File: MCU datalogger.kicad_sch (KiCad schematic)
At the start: 25 parts, among them U1 24LC1025, U2 24LC1025, U3 ATMEGA328P-AU, U4 DS1337S_, Y1 Crystal, Y2 Crystal

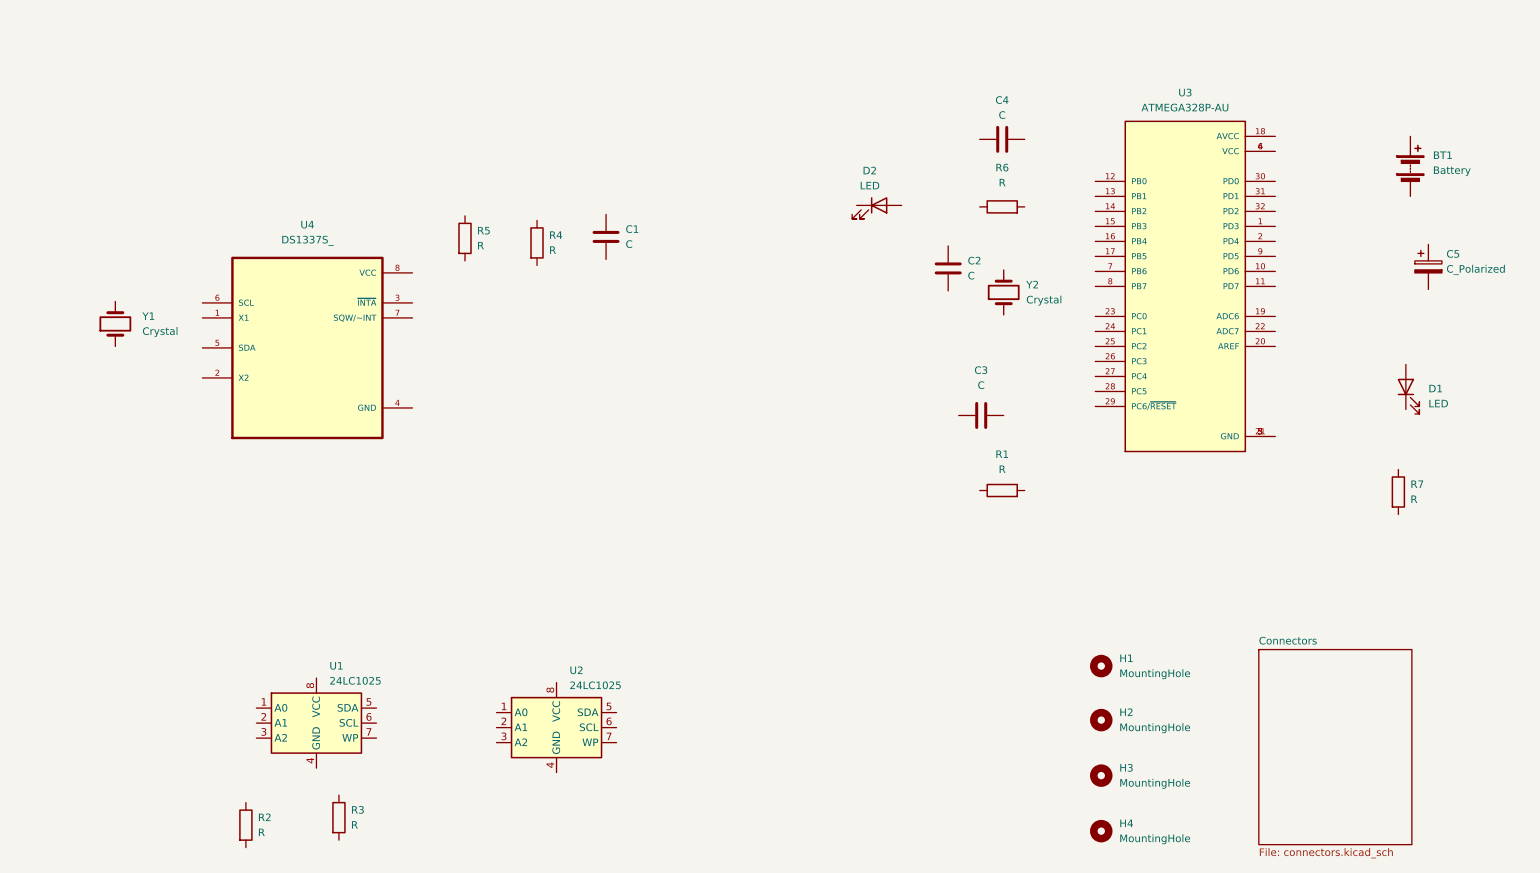
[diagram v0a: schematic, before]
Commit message: value of the compents are added
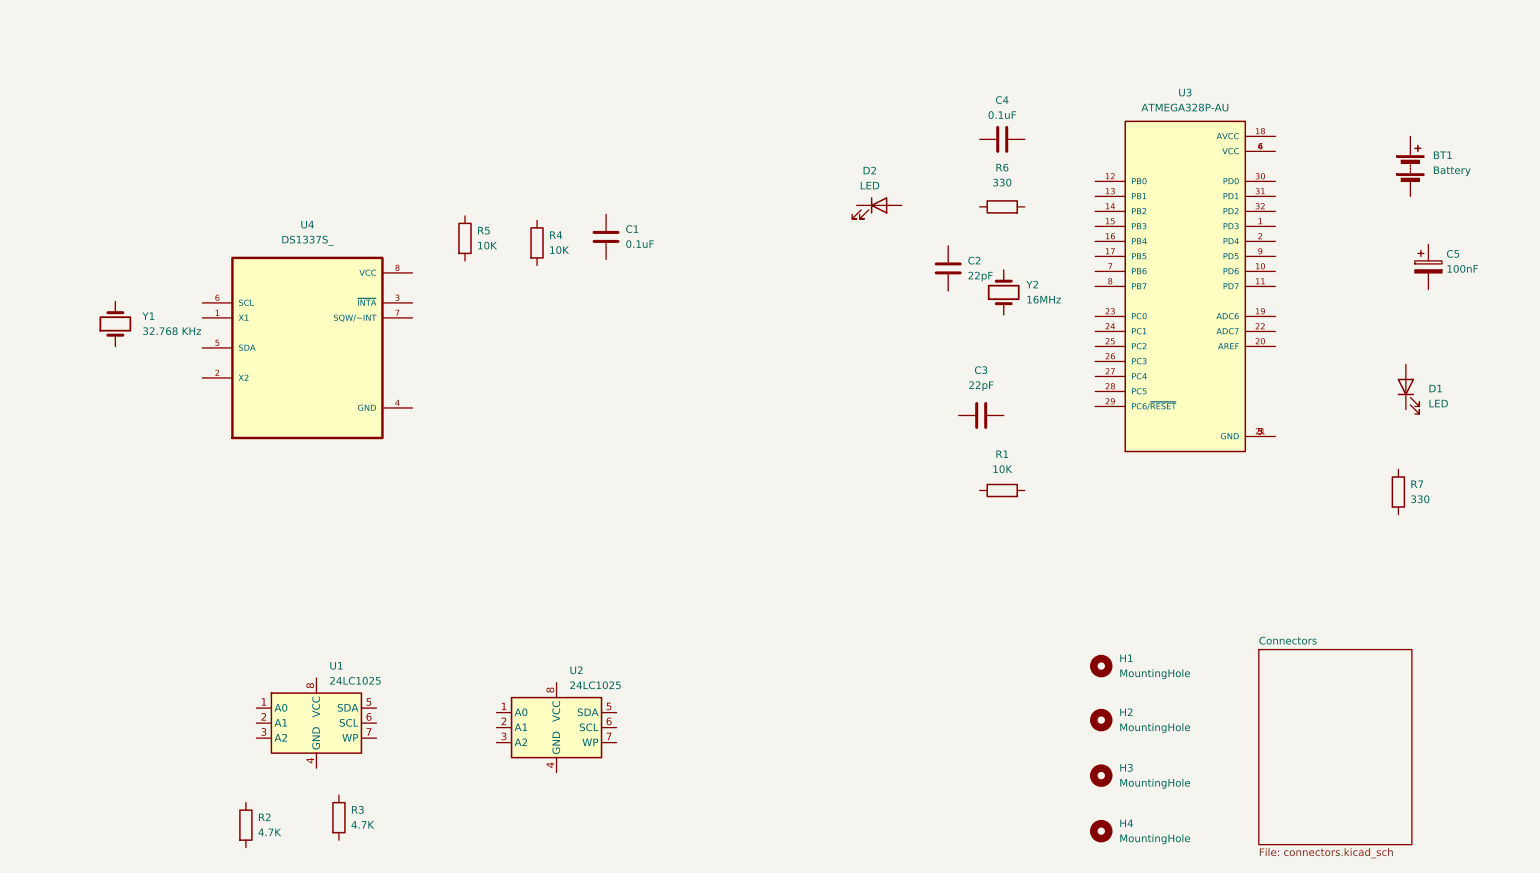
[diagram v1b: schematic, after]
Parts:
- C1, C4: value C -> 0.1uF
- C2, C3: value C -> 22pF
- C5: value C_Polarized -> 100nF
- R1, R4, R5: value R -> 10K
- R2, R3: value R -> 4.7K
- R6, R7: value R -> 330
- Y1: value Crystal -> 32.768 KHz
- Y2: value Crystal -> 16MHz
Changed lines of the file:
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@@
 			)
 		)
-		(property "Value" "C_Polarized"
+		(property "Value" "100nF"
 			(at 274.066 60.8329 0)
 			(effects
@@
 			)
 		)
+		(property "Purpose" ""
+			(at 271.018 60.452 0)
+			(effects
+				(font
+					(size 1.27 1.27)
+				)
+			)
+		)
 		(pin "2"
 		)
@@
 			)
 		)
-		(property "Value" "R"
+		(property "Value" "10K"
 			(at 122.174 57.6579 0)
 			(effects
@@
 			)
 		)
+		(property "Purpose" ""
+			(at 120.142 56.388 0)
+			(effects
+				(font
+					(size 1.27 1.27)
+				)
+			)
+		)
 		(pin "1"
 		)
@@
 			)
 		)
-		(property "Value" "R"
+		(property "Value" "4.7K"
 			(at 88.646 154.9399 0)
 			(effects
@@
 			)
 		)
+		(property "Purpose" ""
+			(at 86.614 153.67 0)
+			(effects
+				(font
+					(size 1.27 1.27)
+				)
+			)
+		)
 		(pin "1"
 		)
@@
 			)
 		)
-		(property "Value" "R"
+		(property "Value" "10K"
 			(at 109.982 56.8959 0)
 			(effects
@@
 			)
 		)
+		(property "Purpose" ""
+			(at 107.95 55.626 0)
+			(effects
+				(font
+					(size 1.27 1.27)
+				)
+			)
+		)
 		(pin "1"
 		)
@@
 			)
 		)
-		(property "Value" "Crystal"
+		(property "Value" "16MHz"
 			(at 202.946 66.0399 90)
 			(effects
@@
 			)
 		)
+		(property "Purpose" ""
+			(at 199.136 64.77 0)
+			(effects
+				(font
+					(size 1.27 1.27)
+				)
+			)
+		)
 		(pin "2"
 		)
@@
 			)
 		)
-		(property "Value" "C"
+		(property "Value" "0.1uF"
 			(at 135.128 56.6419 0)
 			(effects
@@
 			)
 		)
+		(property "Purpose" ""
+			(at 131.826 55.372 0)
+			(effects
+				(font
+					(size 1.27 1.27)
+				)
+			)
+		)
 		(pin "2"
 		)
@@
 			)
 		)
-		(property "Value" "R"
+		(property "Value" "10K"
 			(at 198.882 94.742 90)
 			(effects
@@
 			)
 		)
+		(property "Purpose" ""
+			(at 198.882 98.298 0)
+			(effects
+				(font
+					(size 1.27 1.27)
+				)
+			)
+		)
 		(pin "1"
 		)
@@
 			)
 		)
-		(property "Value" "C"
+		(property "Value" "0.1uF"
 			(at 198.882 34.798 90)
 			(effects
@@
 			)
 		)
+		(property "Purpose" ""
+			(at 198.882 38.862 0)
+			(effects
+				(font
+					(size 1.27 1.27)
+				)
+			)
+		)
 		(pin "2"
 		)
@@
 			)
 		)
-		(property "Value" "R"
+		(property "Value" "330"
 			(at 198.882 46.228 90)
 			(effects
@@
 			)
 		)
+		(property "Purpose" ""
+			(at 198.882 50.292 0)
+			(effects
+				(font
+					(size 1.27 1.27)
+				)
+			)
+		)
 		(pin "1"
 		)
@@
 			)
 		)
-		(property "Value" "R"
+		(property "Value" "4.7K"
 			(at 72.898 156.2099 0)
 			(effects
@@
 			)
 		)
+		(property "Purpose" ""
+			(at 70.866 154.94 0)
+			(effects
+				(font
+					(size 1.27 1.27)
+				)
+			)
+		)
 		(pin "1"
 		)
@@
 			)
 		)
-		(property "Value" "C"
+		(property "Value" "22pF"
 			(at 195.326 80.518 90)
 			(effects
@@
 			)
 		)
+		(property "Purpose" ""
+			(at 195.326 85.598 0)
+			(effects
+				(font
+					(size 1.27 1.27)
+				)
+			)
+		)
 		(pin "2"
 		)
@@
 			)
 		)
-		(property "Value" "C"
+		(property "Value" "22pF"
 			(at 193.04 61.9759 0)
 			(effects
@@
 			)
 		)
+		(property "Purpose" ""
+			(at 189.738 60.706 0)
+			(effects
+				(font
+					(size 1.27 1.27)
+				)
+			)
+		)
 		(pin "2"
 		)
@@
 			)
 		)
-		(property "Value" "Crystal"
+		(property "Value" "32.768 KHz"
 			(at 53.34 71.3739 90)
 			(effects
@@
 			)
 		)
+		(property "Purpose" ""
+			(at 48.768 70.104 0)
+			(effects
+				(font
+					(size 1.27 1.27)
+				)
+			)
+		)
 		(pin "2"
 		)
@@
 			)
 		)
-		(property "Value" "R"
+		(property "Value" "330"
 			(at 267.97 99.8219 0)
 			(effects
@@
 			)
 		)
+		(property "Purpose" ""
+			(at 265.938 98.552 0)
+			(effects
+				(font
+					(size 1.27 1.27)
+				)
+			)
+		)

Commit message: completed footprint association
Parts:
- BT1: footprint (none) -> Connector_PinHeader_2.54mm:PinHeader_1x02_P2.54mm_Vertical
- C1, C2, C3, C4, C5: footprint (none) -> Capacitor_SMD:C_0805_2012Metric
- D1, D2: footprint (none) -> LED_SMD:LED_0805_2012Metric
- H1, H2, H3, H4: footprint (none) -> MountingHole:MountingHole_2.1mm
- R1, R2, R3, R4, R5, R6, R7: footprint (none) -> Resistor_SMD:R_0805_2012Metric
- U1, U2: footprint (none) -> Package_SO:SOIC-8_5.23x5.23mm_P1.27mm
- Y1, Y2: footprint (none) -> Crystal:Crystal_SMD_5032-2Pin_5.0x3.2mm_HandSoldering
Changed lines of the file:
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@@
 			)
 		)
-		(property "Footprint" ""
+		(property "Footprint" "MountingHole:MountingHole_2.1mm"
 			(at 215.646 155.956 0)
 			(effects
@@
 			)
 		)
-		(property "Footprint" ""
+		(property "Footprint" "Capacitor_SMD:C_0805_2012Metric"
 			(at 271.9832 64.262 0)
 			(effects
@@
 			)
 		)
-		(property "Footprint" ""
+		(property "Footprint" "Resistor_SMD:R_0805_2012Metric"
 			(at 118.364 56.388 90)
 			(effects
@@
 			)
 		)
-		(property "Footprint" ""
+		(property "Footprint" "Package_SO:SOIC-8_5.23x5.23mm_P1.27mm"
 			(at 82.804 137.668 0)
 			(effects
@@
 			)
 		)
-		(property "Footprint" ""
+		(property "Footprint" "MountingHole:MountingHole_2.1mm"
 			(at 215.646 146.558 0)
 			(effects
@@
 			)
 		)
-		(property "Footprint" ""
+		(property "Footprint" "Package_SO:SOIC-8_5.23x5.23mm_P1.27mm"
 			(at 123.444 138.43 0)
 			(effects
@@
 			)
 		)
-		(property "Footprint" ""
+		(property "Footprint" "MountingHole:MountingHole_2.1mm"
 			(at 215.646 128.016 0)
 			(effects
@@
 			)
 		)
-		(property "Footprint" ""
+		(property "Footprint" "Resistor_SMD:R_0805_2012Metric"
 			(at 84.836 153.67 90)
 			(effects
@@
 			)
 		)
-		(property "Footprint" ""
+		(property "Footprint" "Resistor_SMD:R_0805_2012Metric"
 			(at 106.172 55.626 90)
 			(effects
@@
 			)
 		)
-		(property "Footprint" ""
+		(property "Footprint" "Crystal:Crystal_SMD_5032-2Pin_5.0x3.2mm_HandSoldering"
 			(at 199.136 64.77 0)
 			(effects
@@
 			)
 		)
-		(property "Footprint" ""
+		(property "Footprint" "Capacitor_SMD:C_0805_2012Metric"
 			(at 132.7912 59.182 0)
 			(effects
@@
 			)
 		)
-		(property "Footprint" ""
+		(property "Footprint" "Resistor_SMD:R_0805_2012Metric"
 			(at 198.882 100.076 90)
 			(effects
@@
 			)
 		)
-		(property "Footprint" ""
+		(property "Footprint" "Capacitor_SMD:C_0805_2012Metric"
 			(at 202.692 37.8968 0)
 			(effects
@@
 			)
 		)
-		(property "Footprint" ""
+		(property "Footprint" "Resistor_SMD:R_0805_2012Metric"
 			(at 198.882 52.07 90)
 			(effects
@@
 			)
 		)
-		(property "Footprint" ""
+		(property "Footprint" "Connector_PinHeader_2.54mm:PinHeader_1x02_P2.54mm_Vertical"
 			(at 267.97 41.91 90)
 			(effects
@@
 			)
 		)
-		(property "Footprint" ""
+		(property "Footprint" "Resistor_SMD:R_0805_2012Metric"
 			(at 69.088 154.94 90)
 			(effects
@@
 			)
 		)
-		(property "Footprint" ""
+		(property "Footprint" "Capacitor_SMD:C_0805_2012Metric"
 			(at 199.136 84.6328 0)
 			(effects
@@
 			)
 		)
-		(property "Footprint" ""
+		(property "Footprint" "LED_SMD:LED_0805_2012Metric"
 			(at 178.054 50.038 0)
 			(effects
@@
 			)
 		)
-		(property "Footprint" ""
+		(property "Footprint" "Capacitor_SMD:C_0805_2012Metric"
 			(at 190.7032 64.516 0)
 			(effects
@@
 			)
 		)
-		(property "Footprint" ""
+		(property "Footprint" "MountingHole:MountingHole_2.1mm"
 			(at 215.646 137.16 0)
 			(effects
@@
 			)
 		)
-		(property "Footprint" ""
+		(property "Footprint" "LED_SMD:LED_0805_2012Metric"
 			(at 267.208 80.772 0)
 			(effects
@@
 			)
 		)
-		(property "Footprint" ""
+		(property "Footprint" "Crystal:Crystal_SMD_5032-2Pin_5.0x3.2mm_HandSoldering"
 			(at 48.768 70.104 0)
 			(effects
@@
 			)
 		)
-		(property "Footprint" ""
+		(property "Footprint" "Resistor_SMD:R_0805_2012Metric"
 			(at 264.16 98.552 90)
 			(effects

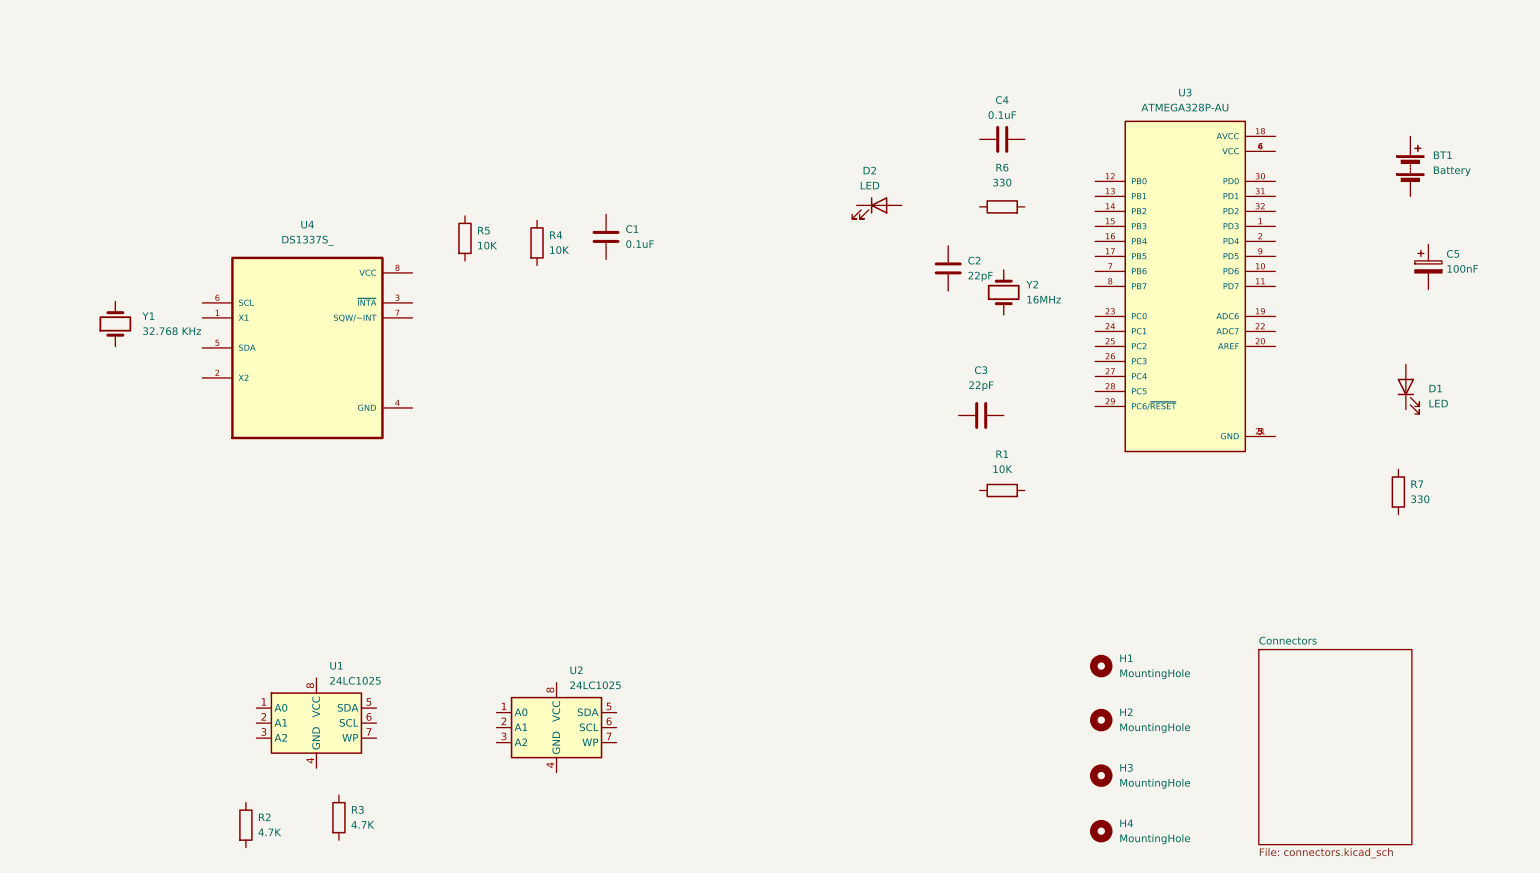
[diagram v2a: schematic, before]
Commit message: Wires and connected
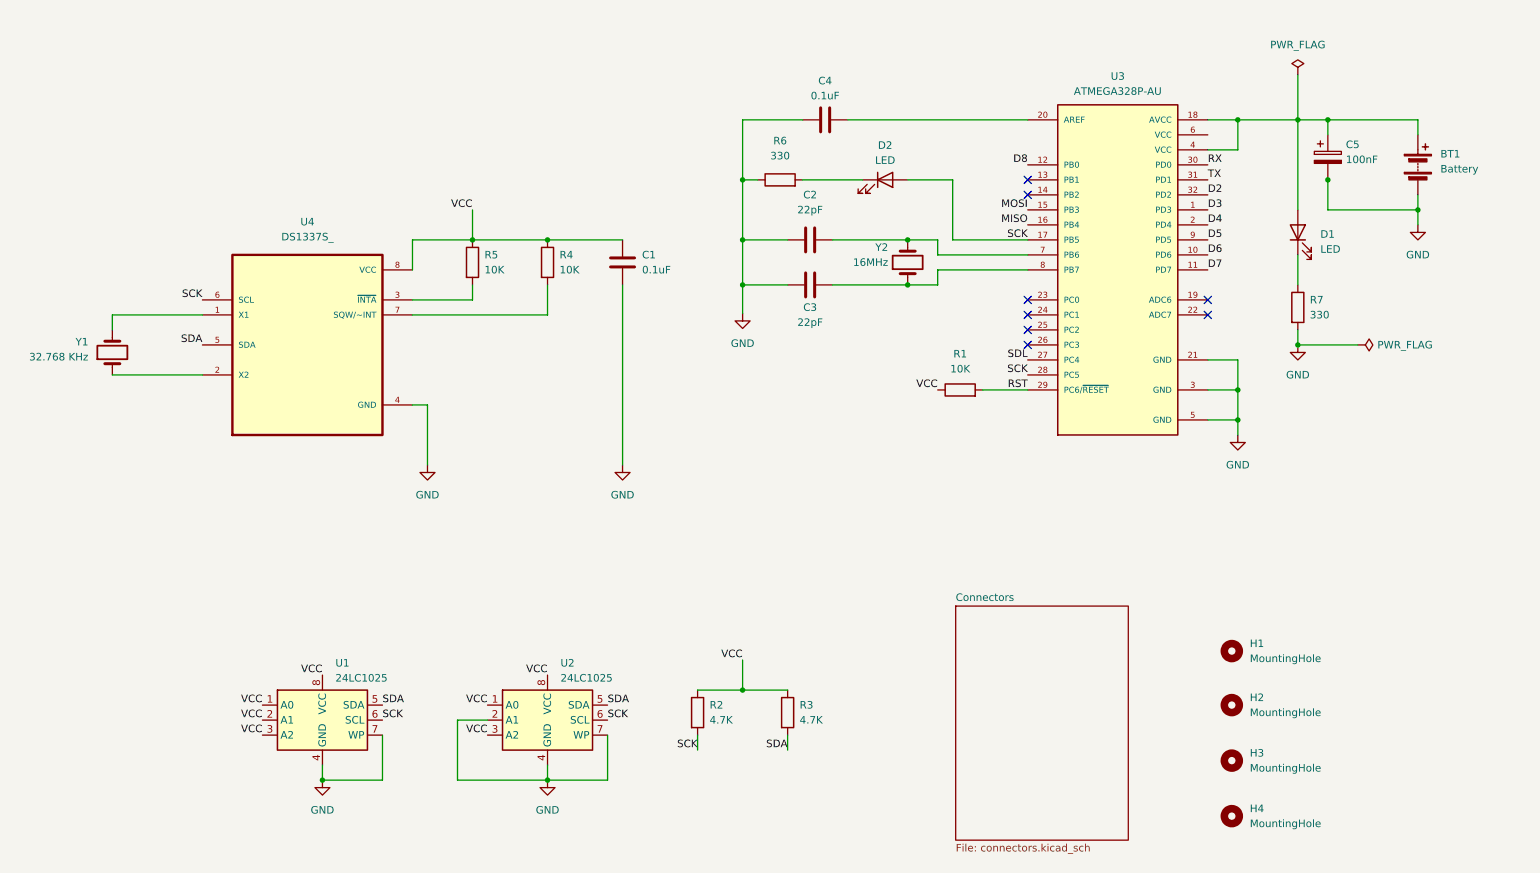
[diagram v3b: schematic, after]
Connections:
- net at U4.1 (X1): now also Y1.2
- net at U4.2 (X2): now also Y1.1
- net at U4.3 (~{INTA}): now also R5.2
- net GND: now reaches U4.4 (GND)
- net GND: now also BT1.2 (-), C1.2, C2.1, C3.1, C4.1, C5.2, R6.1, R7.2, U1.4 (GND), U1.7 (WP), U2.2 (A1), U2.4 (GND), U2.7 (WP), U3.21 (GND), U3.3 (GND), U3.5 (GND)
- net SDA: now reaches U4.5 (SDA)
- net SDA: now also R3.2, U1.5 (SDA), U2.5 (SDA)
- net SCK: now reaches U4.6 (SCL)
- net SCK: now also D2.2 (A), R2.2, U1.6 (SCL), U2.6 (SCL), U3.17 (PB5), U3.28 (PC5)
- net at U4.7 (SQW/~INT): now also R4.2
- net VCC: now reaches U4.8 (VCC)
- net VCC: now also C1.1, R1.1, R2.1, R3.1, R4.1, R5.1, U1.1 (A0), U1.2 (A1), U1.3 (A2), U1.8 (VCC), U2.1 (A0), U2.3 (A2), U2.8 (VCC)
- net at C5.1: now also BT1.1 (+), D1.2 (A), U3.18 (AVCC), U3.4 (VCC)
- net D3: now reaches U3.1 (PD3)
- net D6: now reaches U3.10 (PD6)
- net D7: now reaches U3.11 (PD7)
- net D8: now reaches U3.12 (PB0)
- net MOSI: now reaches U3.15 (PB3)
- net MISO: now reaches U3.16 (PB4)
- net D4: now reaches U3.2 (PD4)
- net at U3.20 (AREF): now also C4.2
- net SDL: now reaches U3.27 (PC4)
- net RST: now reaches U3.29 (PC6/~{RESET})
- net RST: now also R1.2
- net RX: now reaches U3.30 (PD0)
- net TX: now reaches U3.31 (PD1)
- net D2: now reaches U3.32 (PD2)
- net at U3.6 (VCC): no longer U3.4 (VCC)
- net at U3.7 (PB6): now also C2.2, Y2.2
- net at U3.8 (PB7): now also C3.2, Y2.1
- net D5: now reaches U3.9 (PD5)
- net at R6.2: now also D2.1 (K)
- net at D1.1 (K): now also R7.1
- no-connect marks 0 -> 8
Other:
- moved on the sheet: BT1, C1, C2, C3, C4, C5, D1, D2, H1, H2, H3, H4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
